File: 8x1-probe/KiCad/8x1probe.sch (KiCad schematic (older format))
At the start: 50 parts

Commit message: 8x1 probe schematic "done"
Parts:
- removed P? (x7): DEV_1, symbol CONN_01X02
- removed P? (x7): DEV_2, symbol CONN_01X02
- removed P? (x7): DEV_3, symbol CONN_01X02
- removed P? (x7): TC_L, symbol CONN_01X02
- removed P? (x7): DEV_4, symbol CONN_01X02
- removed P? (x7): TC_R, symbol CONN_01X02
- removed P?: TC_I, symbol CONN_02X08
- removed P?: TC_V, symbol CONN_02X08
- added P?: Connector E, symbol CONN_02X10
- added P? (x7): DEV_1, symbol CONN_01X02
- added P? (x7): DEV_2, symbol CONN_01X02
- added P? (x7): DEV_3, symbol CONN_01X02
- added P? (x7): TC_L, symbol CONN_01X02
- added P? (x7): DEV_4, symbol CONN_01X02
- added P? (x7): TC_R, symbol CONN_01X02
- added P?: Connector A, symbol CONN_02X10
- added P?: Connector F, symbol CONN_02X10
- added P?: Connector B, symbol CONN_02X10
- added P?: Connector G, symbol CONN_02X10
- added P?: Connector C, symbol CONN_02X10
- added P?: Connector H, symbol CONN_02X10
- added P?: Connector D, symbol CONN_02X10
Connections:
- net at P?.1 (P1): now also P?.3 (P3)
- net at P?.2 (P2): now also P?.4 (P4)
- net at P?.1 (P1): now also P?.11 (P11)
- net at P?.2 (P2): now also P?.12 (P12)
- net at P?.1 (P1): now also P?.17 (P17)
- net at P?.2 (P2): now also P?.18 (P18)
- net at P?.1 (P1): now also P?.9 (P9)
- net at P?.2 (P2): now also P?.10 (P10)
- net EL_I: no longer names the net of P?.2 (P2)
- net EL_I: now also P?.2 (P2); no longer P?.2 (P2)
- net ER_V: no longer names the net of P?.1 (P1)
- net ER_V: now also P?.1 (P1); no longer P?.1 (P1)
- new net: P?.1 (P1), P?.19 (P19) (x8)
- new net: P?.2 (P2), P?.20 (P20) (x8)
- new net: P?.1 (P1), P?.3 (P3) (x7)
- new net: P?.2 (P2), P?.4 (P4) (x7)
- new net: P?.1 (P1), P?.11 (P11) (x7)
- new net: P?.12 (P12), P?.2 (P2) (x7)
- new net: P?.1 (P1), P?.17 (P17) (x7)
- new net: P?.18 (P18), P?.2 (P2) (x7)
- new net: P?.1 (P1), P?.1 (P1) (x7)
- new net: P?.2 (P2), P?.2 (P2) (x7)
- new net: P?.1 (P1), P?.9 (P9) (x7)
- new net: P?.10 (P10), P?.2 (P2) (x7)
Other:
- moved on the sheet: P?

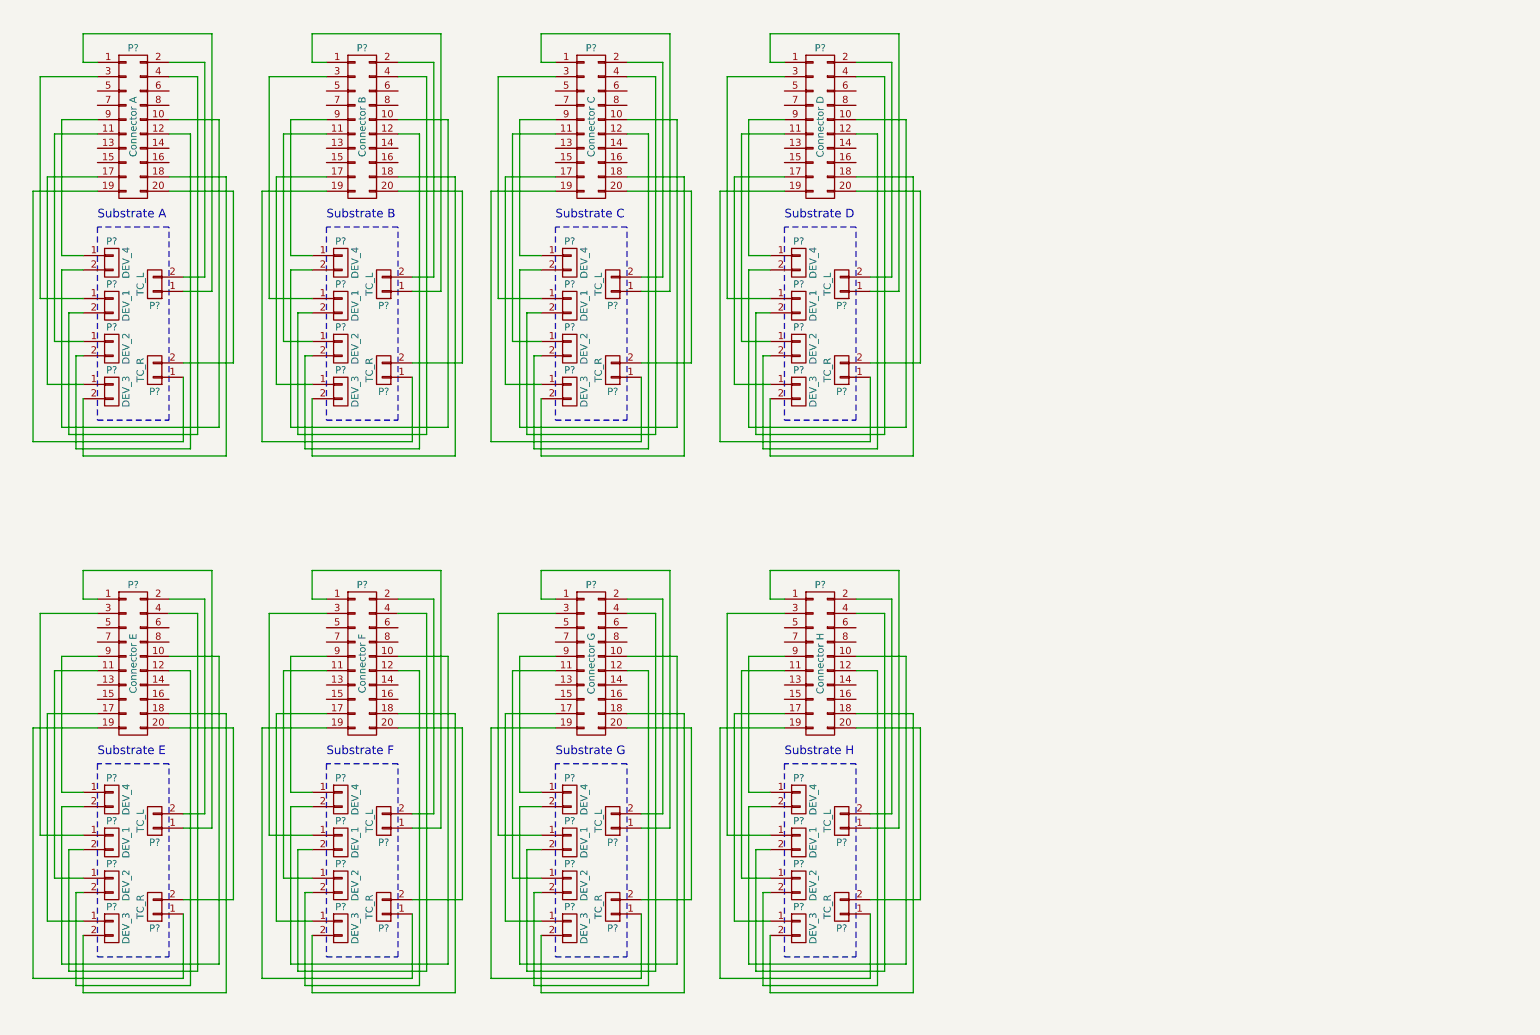
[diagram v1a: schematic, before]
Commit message: single board prototype design almost done need to finish routing
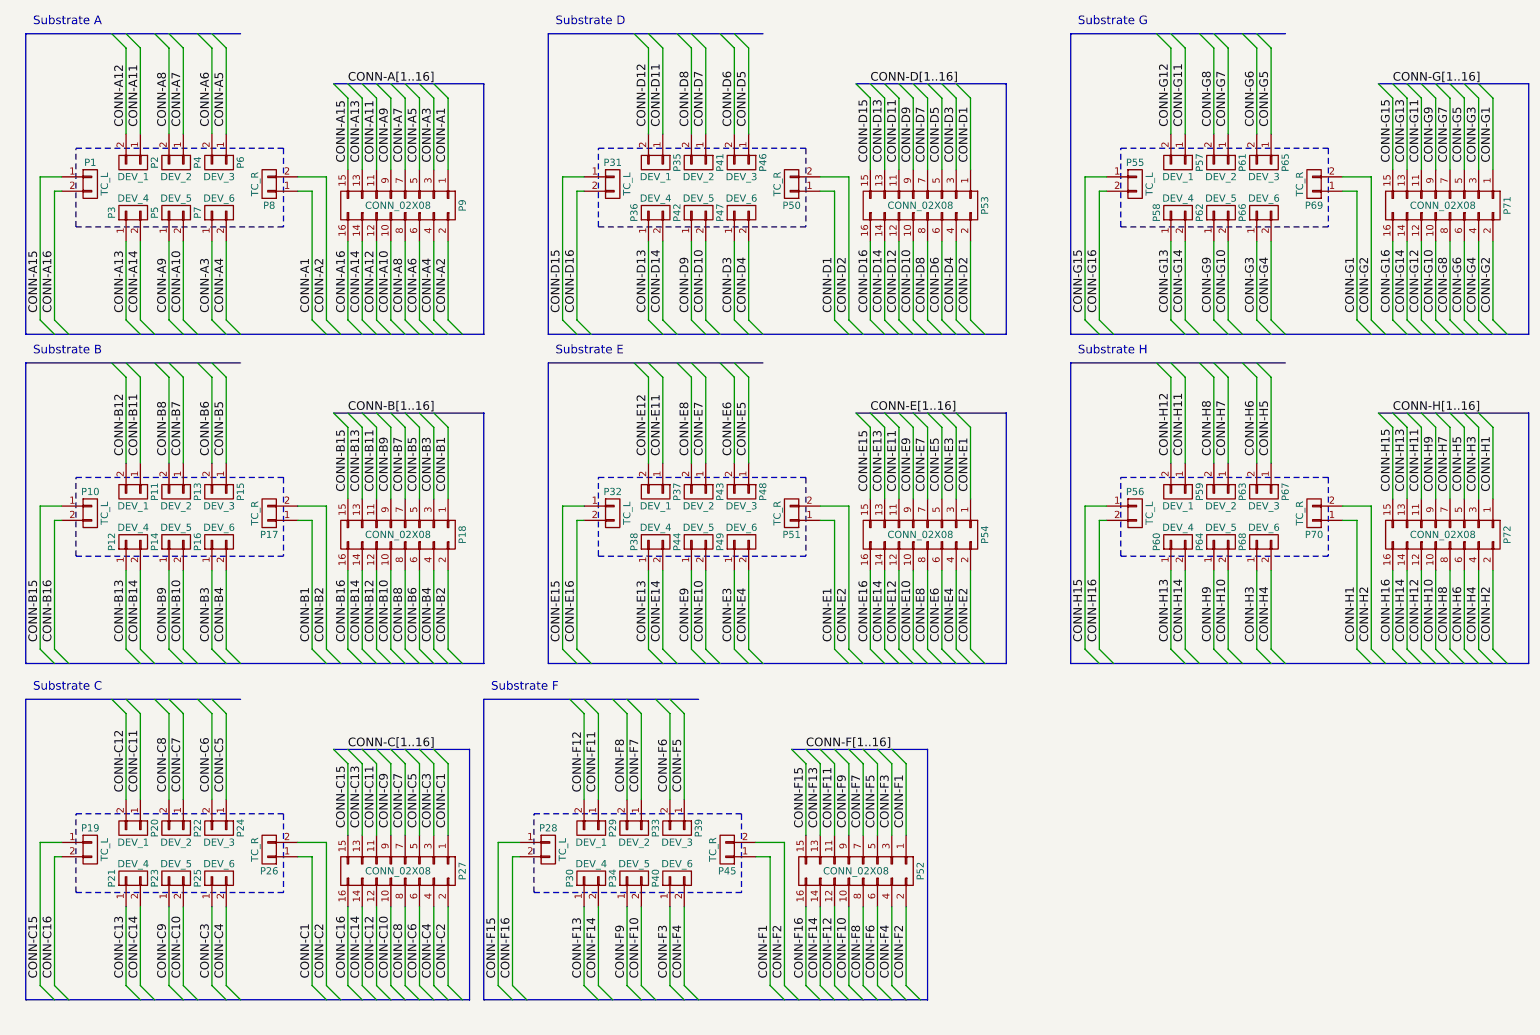
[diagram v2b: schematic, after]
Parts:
- removed P? (x8): DEV_1, symbol CONN_01X02
- removed P? (x8): DEV_2, symbol CONN_01X02
- removed P? (x8): DEV_3, symbol CONN_01X02
- removed P? (x8): TC_L, symbol CONN_01X02
- removed P? (x8): DEV_4, symbol CONN_01X02
- removed P? (x8): TC_R, symbol CONN_01X02
- removed P?: Connector E, symbol CONN_02X10
- removed P?: Connector A, symbol CONN_02X10
- removed P?: Connector F, symbol CONN_02X10
- removed P?: Connector B, symbol CONN_02X10
- removed P?: Connector G, symbol CONN_02X10
- removed P?: Connector C, symbol CONN_02X10
- removed P?: Connector H, symbol CONN_02X10
- removed P?: Connector D, symbol CONN_02X10
- added P1, P10, P11, P12, P13, P14, P15, P16, P17, P19, P2, P20, P21, P22, P23, P24, P25, P26, P28, P29, P3, P30, P31, P32, P33, P34, P35, P36, P37, P38, P39, P4, P40, P41, P42, P43, P44, P45, P46, P47, P48, P49, P5, P50, P51, P55, P56, P57, P58, P59, P6, P60, P61, P62, P63, P64, P65, P66, P67, P68, P69, P7, P70, P8: 2x1_pogo_pin, myparts:2x1_pogo_pin, symbol 2x1_pogo_pin
- added P18, P27, P52, P53, P54, P71, P72, P9: CONN_02X08, Socket_Strips:Socket_Strip_Straight_2x08, symbol CONN_02X08
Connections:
- new net CONN-A1: P8.1 (P1), P9.1 (P1)
- new net CONN-A10: P5.2 (P2), P9.10 (P10)
- new net CONN-A11: P2.1 (P1), P9.11 (P11)
- new net CONN-A12: P2.2 (P2), P9.12 (P12)
- new net CONN-A13: P3.1 (P1), P9.13 (P13)
- new net CONN-A14: P3.2 (P2), P9.14 (P14)
- new net CONN-A15: P1.1 (P1), P9.15 (P15)
- new net CONN-A16: P1.2 (P2), P9.16 (P16)
- new net CONN-A2: P8.2 (P2), P9.2 (P2)
- new net CONN-A3: P7.1 (P1), P9.3 (P3)
- new net CONN-A4: P7.2 (P2), P9.4 (P4)
- new net CONN-A5: P6.1 (P1), P9.5 (P5)
- new net CONN-A6: P6.2 (P2), P9.6 (P6)
- new net CONN-A7: P4.1 (P1), P9.7 (P7)
- new net CONN-A8: P4.2 (P2), P9.8 (P8)
- new net CONN-A9: P5.1 (P1), P9.9 (P9)
- new net CONN-B1: P17.1 (P1), P18.1 (P1)
- new net CONN-B10: P14.2 (P2), P18.10 (P10)
- new net CONN-B11: P11.1 (P1), P18.11 (P11)
- new net CONN-B12: P11.2 (P2), P18.12 (P12)
- new net CONN-B13: P12.1 (P1), P18.13 (P13)
- new net CONN-B14: P12.2 (P2), P18.14 (P14)
- new net CONN-B15: P10.1 (P1), P18.15 (P15)
- new net CONN-B16: P10.2 (P2), P18.16 (P16)
- new net CONN-B2: P17.2 (P2), P18.2 (P2)
- new net CONN-B3: P16.1 (P1), P18.3 (P3)
- new net CONN-B4: P16.2 (P2), P18.4 (P4)
- new net CONN-B5: P15.1 (P1), P18.5 (P5)
- new net CONN-B6: P15.2 (P2), P18.6 (P6)
- new net CONN-B7: P13.1 (P1), P18.7 (P7)
- new net CONN-B8: P13.2 (P2), P18.8 (P8)
- new net CONN-B9: P14.1 (P1), P18.9 (P9)
- new net CONN-C1: P26.1 (P1), P27.1 (P1)
- new net CONN-C10: P23.2 (P2), P27.10 (P10)
- new net CONN-C11: P20.1 (P1), P27.11 (P11)
- new net CONN-C12: P20.2 (P2), P27.12 (P12)
- new net CONN-C13: P21.1 (P1), P27.13 (P13)
- new net CONN-C14: P21.2 (P2), P27.14 (P14)
- new net CONN-C15: P19.1 (P1), P27.15 (P15)
- new net CONN-C16: P19.2 (P2), P27.16 (P16)
- new net CONN-C2: P26.2 (P2), P27.2 (P2)
- new net CONN-C3: P25.1 (P1), P27.3 (P3)
- new net CONN-C4: P25.2 (P2), P27.4 (P4)
- new net CONN-C5: P24.1 (P1), P27.5 (P5)
- new net CONN-C6: P24.2 (P2), P27.6 (P6)
- new net CONN-C7: P22.1 (P1), P27.7 (P7)
- new net CONN-C8: P22.2 (P2), P27.8 (P8)
- new net CONN-C9: P23.1 (P1), P27.9 (P9)
- new net CONN-D1: P50.1 (P1), P53.1 (P1)
- new net CONN-D10: P42.2 (P2), P53.10 (P10)
- new net CONN-D11: P35.1 (P1), P53.11 (P11)
- new net CONN-D12: P35.2 (P2), P53.12 (P12)
- new net CONN-D13: P36.1 (P1), P53.13 (P13)
- new net CONN-D14: P36.2 (P2), P53.14 (P14)
- new net CONN-D15: P31.1 (P1), P53.15 (P15)
- new net CONN-D16: P31.2 (P2), P53.16 (P16)
- new net CONN-D2: P50.2 (P2), P53.2 (P2)
- new net CONN-D3: P47.1 (P1), P53.3 (P3)
- new net CONN-D4: P47.2 (P2), P53.4 (P4)
- new net CONN-D5: P46.1 (P1), P53.5 (P5)
- new net CONN-D6: P46.2 (P2), P53.6 (P6)
- new net CONN-D7: P41.1 (P1), P53.7 (P7)
- new net CONN-D8: P41.2 (P2), P53.8 (P8)
- new net CONN-D9: P42.1 (P1), P53.9 (P9)
- new net CONN-E1: P51.1 (P1), P54.1 (P1)
- new net CONN-E10: P44.2 (P2), P54.10 (P10)
- new net CONN-E11: P37.1 (P1), P54.11 (P11)
- new net CONN-E12: P37.2 (P2), P54.12 (P12)
- new net CONN-E13: P38.1 (P1), P54.13 (P13)
- new net CONN-E14: P38.2 (P2), P54.14 (P14)
- new net CONN-E15: P32.1 (P1), P54.15 (P15)
- new net CONN-E16: P32.2 (P2), P54.16 (P16)
- new net CONN-E2: P51.2 (P2), P54.2 (P2)
- new net CONN-E3: P49.1 (P1), P54.3 (P3)
- new net CONN-E4: P49.2 (P2), P54.4 (P4)
- new net CONN-E5: P48.1 (P1), P54.5 (P5)
- new net CONN-E6: P48.2 (P2), P54.6 (P6)
- new net CONN-E7: P43.1 (P1), P54.7 (P7)
- new net CONN-E8: P43.2 (P2), P54.8 (P8)
- new net CONN-E9: P44.1 (P1), P54.9 (P9)
- new net CONN-F1: P45.1 (P1), P52.1 (P1)
- new net CONN-F10: P34.2 (P2), P52.10 (P10)
- new net CONN-F11: P29.1 (P1), P52.11 (P11)
- new net CONN-F12: P29.2 (P2), P52.12 (P12)
- new net CONN-F13: P30.1 (P1), P52.13 (P13)
- new net CONN-F14: P30.2 (P2), P52.14 (P14)
- new net CONN-F15: P28.1 (P1), P52.15 (P15)
- new net CONN-F16: P28.2 (P2), P52.16 (P16)
- new net CONN-F2: P45.2 (P2), P52.2 (P2)
- new net CONN-F3: P40.1 (P1), P52.3 (P3)
- new net CONN-F4: P40.2 (P2), P52.4 (P4)
- new net CONN-F5: P39.1 (P1), P52.5 (P5)
- new net CONN-F6: P39.2 (P2), P52.6 (P6)
- new net CONN-F7: P33.1 (P1), P52.7 (P7)
- new net CONN-F8: P33.2 (P2), P52.8 (P8)
- new net CONN-F9: P34.1 (P1), P52.9 (P9)
- new net CONN-G1: P69.1 (P1), P71.1 (P1)
- new net CONN-G10: P62.2 (P2), P71.10 (P10)
- new net CONN-G11: P57.1 (P1), P71.11 (P11)
- new net CONN-G12: P57.2 (P2), P71.12 (P12)
- new net CONN-G13: P58.1 (P1), P71.13 (P13)
- new net CONN-G14: P58.2 (P2), P71.14 (P14)
- new net CONN-G15: P55.1 (P1), P71.15 (P15)
- new net CONN-G16: P55.2 (P2), P71.16 (P16)
- new net CONN-G2: P69.2 (P2), P71.2 (P2)
- new net CONN-G3: P66.1 (P1), P71.3 (P3)
- new net CONN-G4: P66.2 (P2), P71.4 (P4)
- new net CONN-G5: P65.1 (P1), P71.5 (P5)
- new net CONN-G6: P65.2 (P2), P71.6 (P6)
- new net CONN-G7: P61.1 (P1), P71.7 (P7)
- new net CONN-G8: P61.2 (P2), P71.8 (P8)
- new net CONN-G9: P62.1 (P1), P71.9 (P9)
- new net CONN-H1: P70.1 (P1), P72.1 (P1)
- new net CONN-H10: P64.2 (P2), P72.10 (P10)
- new net CONN-H11: P59.1 (P1), P72.11 (P11)
- new net CONN-H12: P59.2 (P2), P72.12 (P12)
- new net CONN-H13: P60.1 (P1), P72.13 (P13)
- new net CONN-H14: P60.2 (P2), P72.14 (P14)
- new net CONN-H15: P56.1 (P1), P72.15 (P15)
- new net CONN-H16: P56.2 (P2), P72.16 (P16)
- new net CONN-H2: P70.2 (P2), P72.2 (P2)
- new net CONN-H3: P68.1 (P1), P72.3 (P3)
- new net CONN-H4: P68.2 (P2), P72.4 (P4)
- new net CONN-H5: P67.1 (P1), P72.5 (P5)
- new net CONN-H6: P67.2 (P2), P72.6 (P6)
- new net CONN-H7: P63.1 (P1), P72.7 (P7)
- new net CONN-H8: P63.2 (P2), P72.8 (P8)
- new net CONN-H9: P64.1 (P1), P72.9 (P9)
